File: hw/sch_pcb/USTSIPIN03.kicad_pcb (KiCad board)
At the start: 2 copper layers, 70.6 x 50.3 mm, 107 parts, among them J1 HEADER_2x15, M1 HOLE, M2 HOLE, M3 HOLE, M4 HOLE, M5 RFShield_TwoPieces, Q1 2SK2394-6, U1 ISL21080CIH341Z-TK, U10 ISL21080DIH309, U11 AT24CS64-SSHM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

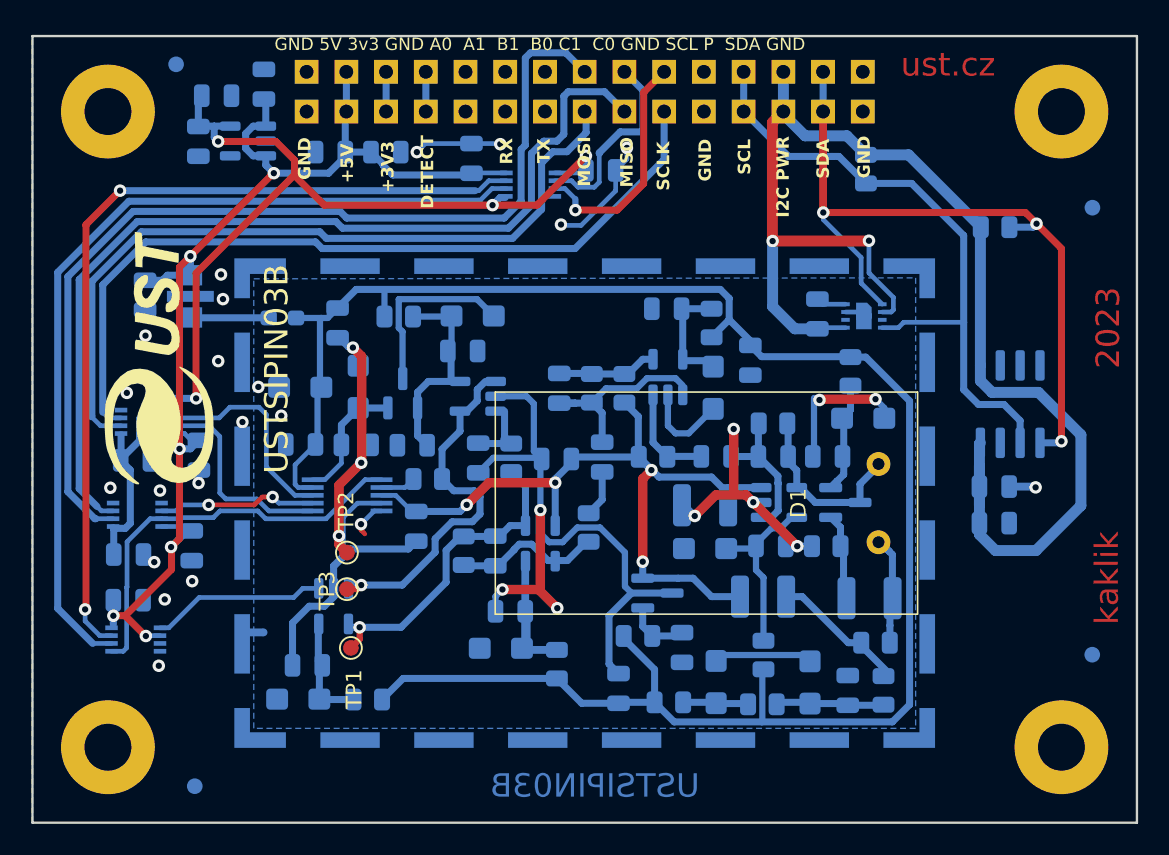
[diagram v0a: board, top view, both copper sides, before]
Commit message: Fix #8 Adding solder jumpers.
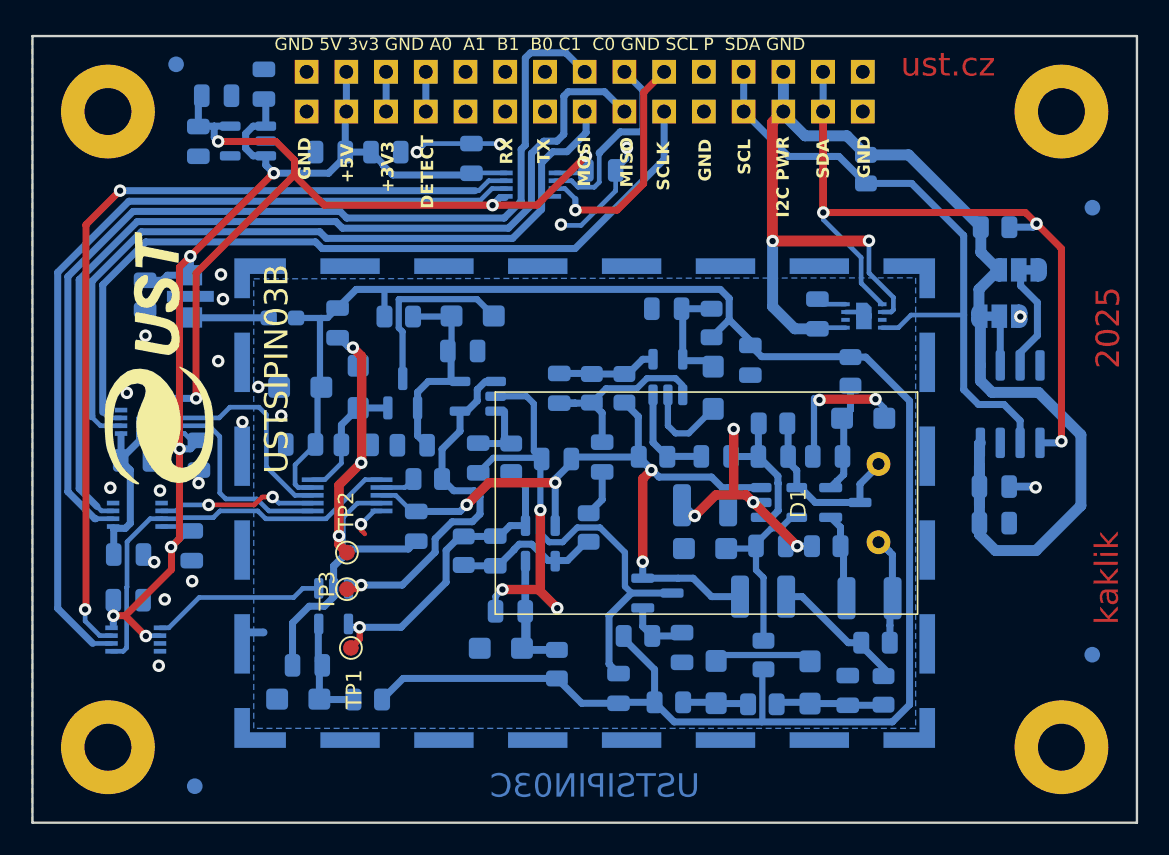
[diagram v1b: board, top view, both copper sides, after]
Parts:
- added JP2: SolderJumper_3_Bridged12, Jumper:SolderJumper-3_P1.3mm_Bridged12_RoundedPad1.0x1.5mm, B.Cu at (175.0, 97.8)
- added JP3: SolderJumper_3_Bridged12, Jumper:SolderJumper-3_P1.3mm_Bridged12_RoundedPad1.0x1.5mm, B.Cu at (176.3, 94.8)
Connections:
- U11 pad 2: GND -> Net-(JP2-C)
- U11 pad 3: GND -> Net-(JP3-C)
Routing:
- net Net-(JP3-C): track 0.00 -> 7.06 mm
- net Net-(JP2-C): track 0.00 -> 3.17 mm
- net VDD: track 87.1 -> 88.1 mm
- net GND: vias 21 -> 22
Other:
- board text added: "2025"
- board text added: "USTSIPIN03C"
- board text removed: "2023"

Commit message: Resolve #10
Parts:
- removed C23, C31: 100nF, Capacitor_SMD:C_0805_2012Metric
- removed C24: 10uF, Capacitor_Tantalum_SMD:CP_EIA-3216-18_Kemet-A
- removed C35: 3n3, Capacitor_SMD:C_0805_2012Metric
- removed R11: 470R, Resistor_SMD:R_0805_2012Metric
- removed R18, R20: 10k, Resistor_SMD:R_0805_2012Metric
- removed R22: 1k, Resistor_SMD:R_0805_2012Metric
- removed U9: AD8691, Package_TO_SOT_SMD:TSOT-23-5
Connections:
- C30 pad 1: Net-(U9-+) -> /PIN_detector/Signal
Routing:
- net Net-(C31-Pad2): track 12.8 -> 0.00 mm
- net Net-(U9-V+): track 7.39 -> 0.00 mm
- net Net-(U9--): track 6.40 -> 0.00 mm
- net Net-(U9-+): track 5.95 -> 0.00 mm
- net /PIN_detector/Signal: track 3.00 -> 8.71 mm
- net GNDA: track 128.5 -> 123.4 mm
- net /PIN_detector/REF: track 51.5 -> 46.4 mm, vias 4 -> 2
- net +5V: track 125.9 -> 123.9 mm

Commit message: Improve layout.
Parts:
- moved C17 5.88 mm to (151.8, 103.9), turned to 90 degrees
- moved C16 5.18 mm to (145.0, 102.8), turned to 90 degrees
- moved C21 2.50 mm to (163.8, 104.2), turned to 180 degrees
- moved R13 2.12 mm to (160.6, 106.7)
- moved R5 0.63 mm to (144.4, 106.8)
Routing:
- net GNDA: track 123.4 -> 119.1 mm, vias 12 -> 10
- net /PIN_detector/A: track 11.8 -> 9.66 mm
- net Net-(C25-Pad1): track 9.49 -> 7.38 mm

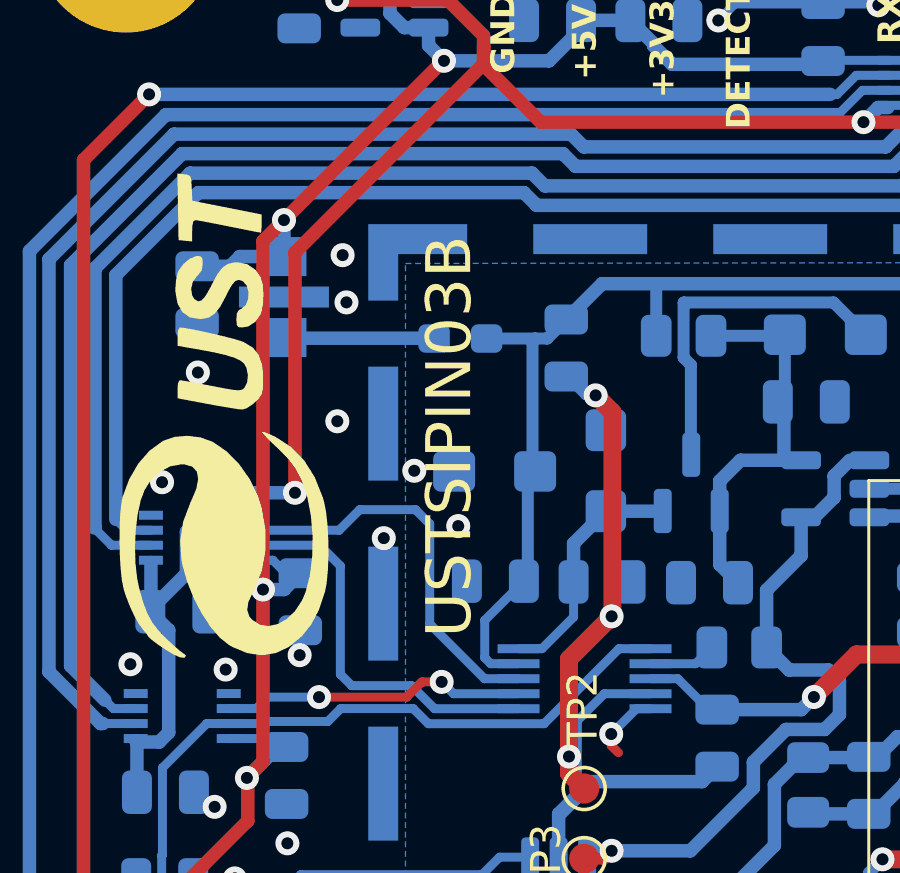
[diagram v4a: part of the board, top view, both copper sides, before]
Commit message: Fix wrong revision in silkscreen.
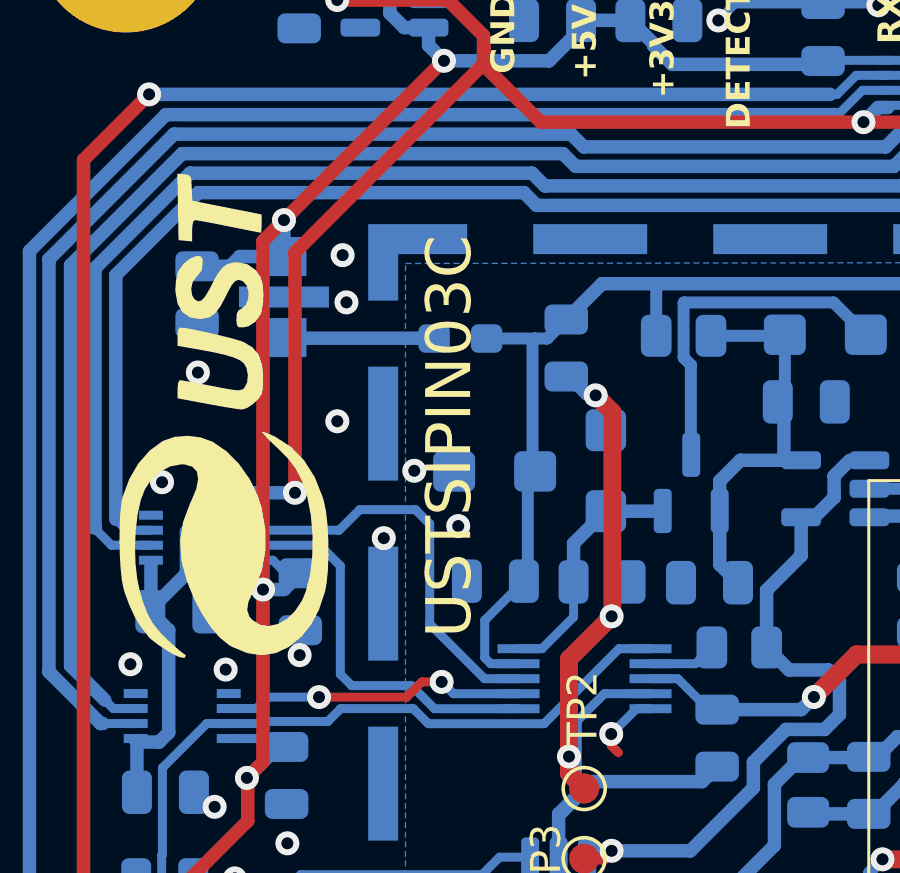
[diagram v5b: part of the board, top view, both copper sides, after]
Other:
- board text removed: "USTSIPIN03B"
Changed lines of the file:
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@@
 		)
 	)
-	(gr_text "USTSIPIN03B"
+	(gr_text "USTSIPIN03C"
 		(at 128.8034 101.1428 90)
 		(layer "F.SilkS")

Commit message: Add dimensioned drawing.
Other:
- board text added: "Radiation Sensing Area"
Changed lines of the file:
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@@
+		)
+	)
+	(gr_text "Radiation Sensing Area"
+		(at 153.162 106.553 0)
+		(layer "Cmts.User")
+		(effects
+			(font
+				(size 1 1)
+				(thickness 0.15)
+			)
 		)
 	)
@@
 			(layer "Cmts.User")
 			(effects
+				(font
+					(size 1 1)
+					(thickness 0.15)
+				)
+			)
+		)
+	)
+	(dimension
+		(type orthogonal)
+		(layer "Cmts.User")
+		(pts
+			(xy 142.7844 102.6136) (xy 169.7844 102.6136)
+		)
+		(height -2.3344)
+		(orientation 0)
+		(format
+			(prefix "")
+			(suffix "")
+			(units 3)
+			(units_format 0)
+			(precision 4)
+			(suppress_zeroes yes)
+		)
+		(style
+			(thickness 0.15)
+			(arrow_length 1.27)
+			(text_position_mode 0)
+			(arrow_direction outward)
+			(extension_height 0.58642)
+			(extension_offset 0.5)
+			(keep_text_aligned yes)
+		)
+		(gr_text "27"
+			(at 156.2844 99.1292 0)
+			(layer "Cmts.User")
+			(effects
+				(font
+					(size 1 1)
+					(thickness 0.15)
+				)
+			)
+		)
+	)
+	(dimension
+		(type orthogonal)
+		(layer "Cmts.User")
+		(pts
+			(xy 118.02 125.32) (xy 142.7844 116.8136)
+		)
+		(height 21.4768)
+		(orientation 1)
+		(format
+			(prefix "")
+			(suffix "")
+			(units 3)
+			(units_format 0)
+			(precision 4)
+			(suppress_zeroes yes)
+		)
+		(style
+			(thickness 0.15)
+			(arrow_length 1.27)
+			(text_position_mode 0)
+			(arrow_direction outward)
+			(extension_height 0.58642)
+			(extension_offset 0.5)
+			(keep_text_aligned yes)
+		)
+		(gr_text "8.5064"
+			(at 138.3468 121.0668 90)
+			(layer "Cmts.User")
+			(effects
+				(font
+					(size 1 1)
+					(thickness 0.15)
+				)
+			)
+		)
+	)
+	(dimension
+		(type orthogonal)
+		(layer "Cmts.User")
+		(pts
+			(xy 169.7844 116.8136) (xy 178.98 125.32)
+		)
+		(height 3.4554)
+		(orientation 0)
+		(format
+			(prefix "")
+			(suffix "")
+			(units 3)
+			(units_format 0)
+			(precision 4)
+			(suppress_zeroes yes)
+		)
+		(style
+			(thickness 0.15)
+			(arrow_length 1.27)
+			(text_position_mode 0)
+			(arrow_direction outward)
+			(extension_height 0.58642)
+			(extension_offset 0.5)
+			(keep_text_aligned yes)
+		)
+		(gr_text "9.1956"
+			(at 174.3822 119.119 0)
+			(layer "Cmts.User")
+			(effects
+				(font
+					(size 1 1)
+					(thickness 0.15)
+				)
+			)
+		)
+	)
+	(dimension
+		(type orthogonal)
+		(layer "Cmts.User")
+		(pts
+			(xy 169.7844 116.8136) (xy 169.7844 102.6136)
+		)
+		(height 3.2658)
+		(orientation 1)
+		(format
+			(prefix "")
+			(suffix "")
+			(units 3)
+			(units_format 0)
+			(precision 4)
+			(suppress_zeroes yes)
+		)
+		(style
+			(thickness 0.15)
+			(arrow_length 1.27)
+			(text_position_mode 0)
+			(arrow_direction outward)
+			(extension_height 0.58642)
+			(extension_offset 0.5)
+			(keep_text_aligned yes)
+		)
+		(gr_text "14.2"
+			(at 171.9002 109.7136 90)
+			(layer "Cmts.User")
+			(effects
+				(font
+					(size 1 1)
+					(thickness 0.15)
+				)
+			)
+		)
+	)
+	(dimension
+		(type orthogonal)
+		(layer "Cmts.User")
+		(pts
+			(xy 113.194 130.145999) (xy 183.806 130.145999)
+		)
+		(height 5.363001)
+		(orientation 0)
+		(format
+			(prefix "")
+			(suffix "")
+			(units 3)
+			(units_format 1)
+			(precision 4)
+			(suppress_zeroes yes)
+		)
+		(style
+			(thickness 0.15)
+			(arrow_length 1.27)
+			(text_position_mode 0)
+			(arrow_direction outward)
+			(extension_height 0.58642)
+			(extension_offset 0.5)
+			(keep_text_aligned yes)
+		)
+		(gr_text "70.612 mm"
+			(at 148.5 134.359 0)
+			(layer "Cmts.User")
+			(effects
+				(font
+					(size 1 1)
+					(thickness 0.15)
+				)
+			)
+		)
+	)
+	(dimension
+		(type orthogonal)
+		(layer "Cmts.User")
+		(pts
+			(xy 113.194 130.145999) (xy 113.194 79.854)
+		)
+		(height -3.847)
+		(orientation 1)
+		(format
+			(prefix "")
+			(suffix "")
+			(units 3)
+			(units_format 1)
+			(precision 4)
+			(suppress_zeroes yes)
+		)
+		(style
+			(thickness 0.15)
+			(arrow_length 1.27)
+			(text_position_mode 0)
+			(arrow_direction outward)
+			(extension_height 0.58642)
+			(extension_offset 0.5)
+			(keep_text_aligned yes)
+		)
+		(gr_text "50.292 mm"
+			(at 108.197 104.999999 90)
+			(layer "Cmts.User")
+			(effects
